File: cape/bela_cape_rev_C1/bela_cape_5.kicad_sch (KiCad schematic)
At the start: 26 parts, among them IC1 TLV320AIC3104, IC2 MIC5317

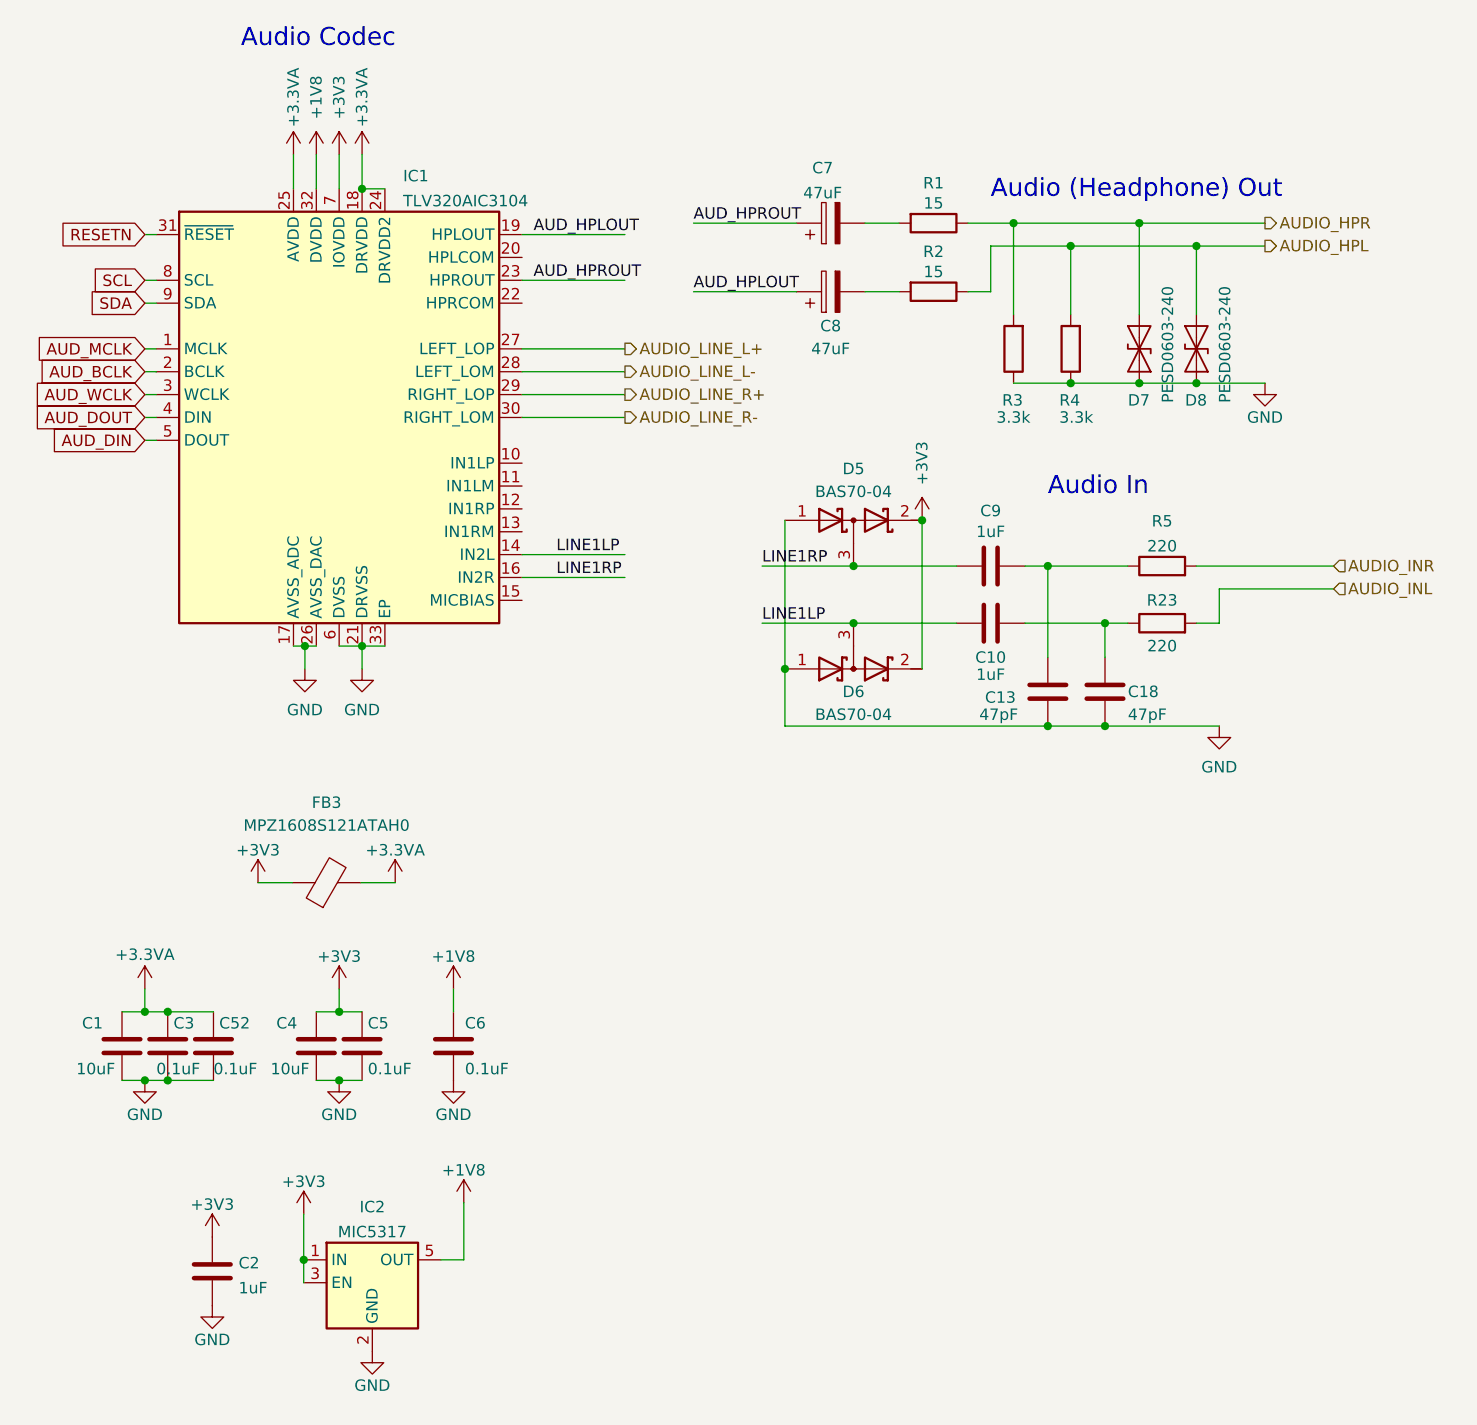
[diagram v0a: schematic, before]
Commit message: More C1 cape routing
(cherry picked from commit db7d999e21b46c22925661ce0002776775f31ffd)
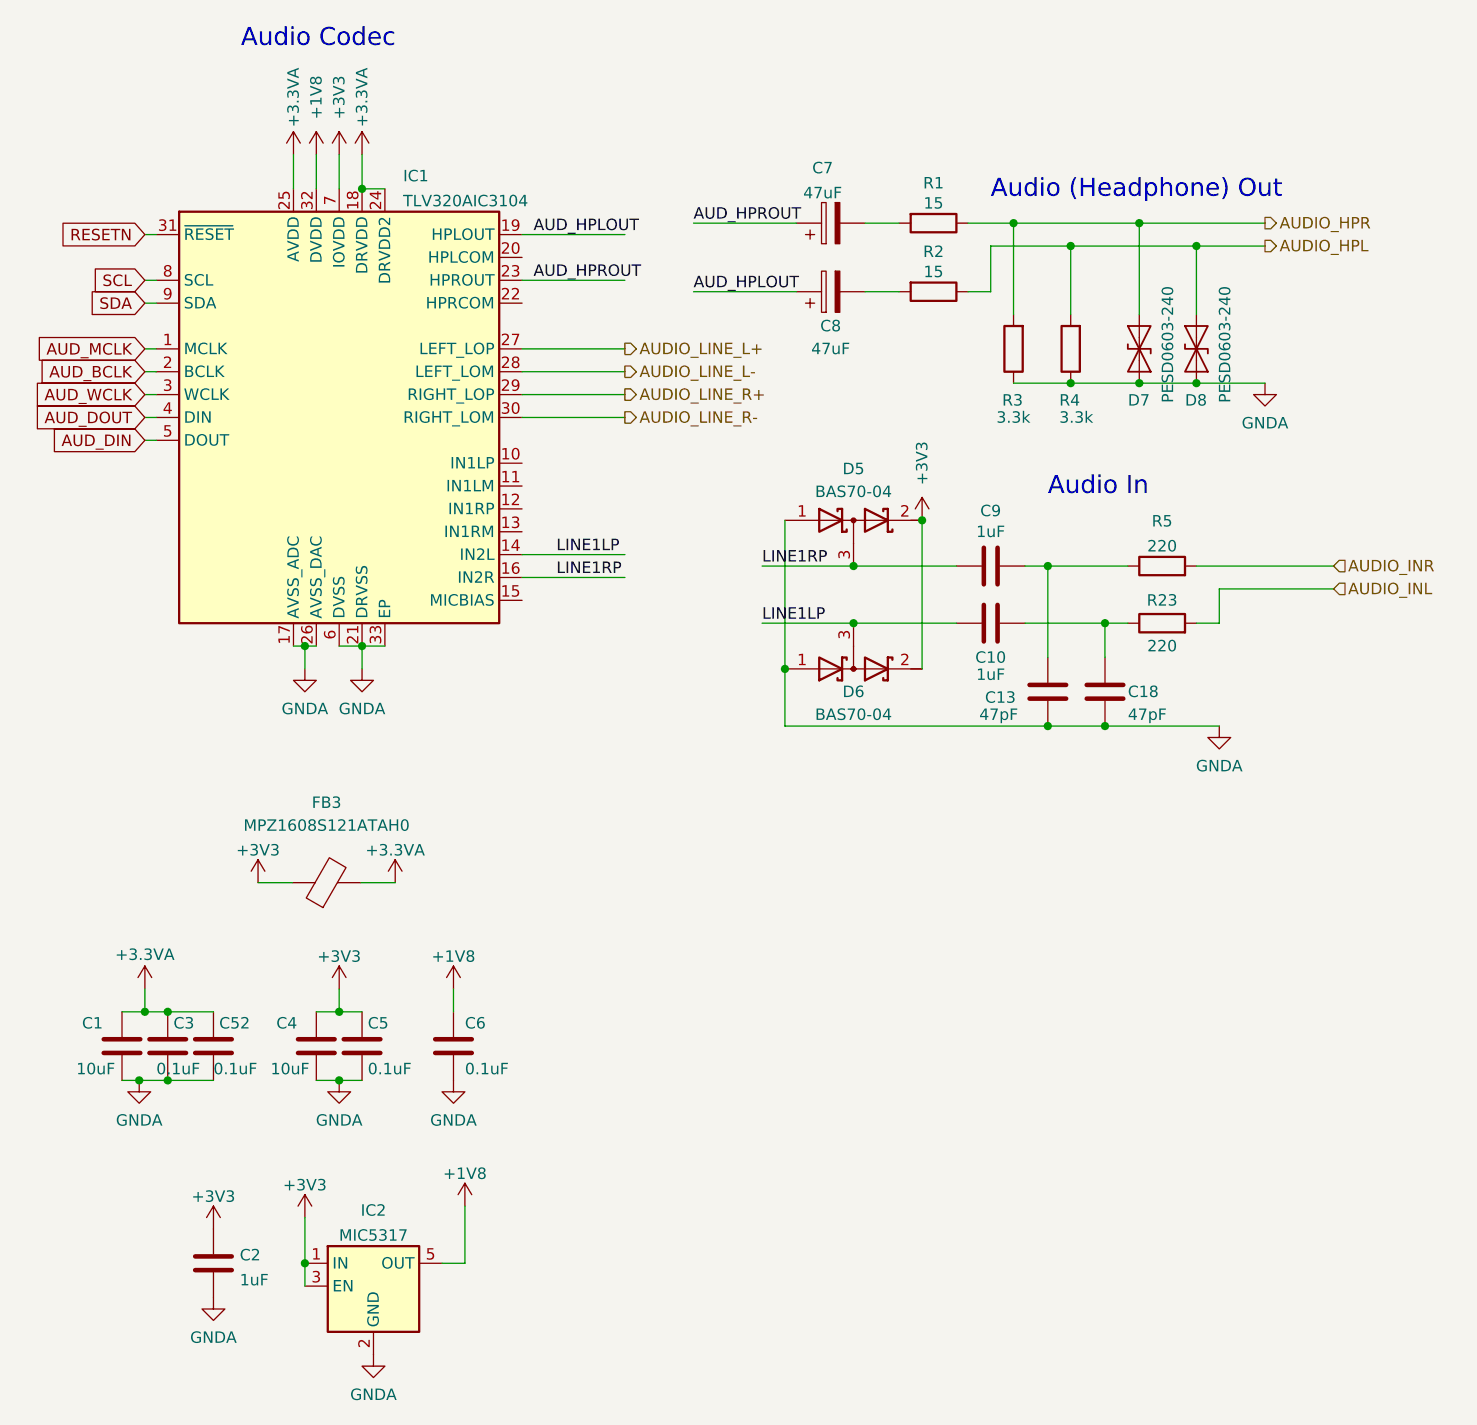
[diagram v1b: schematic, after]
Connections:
- net GND renamed GNDA
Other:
- moved on the sheet: C2

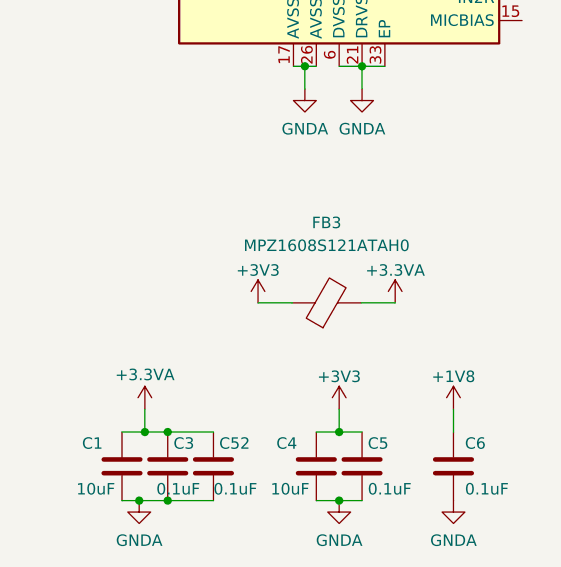
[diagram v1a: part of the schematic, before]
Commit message: Further routing on C1 cape
(cherry picked from commit 232a25b01e013bf194cdc3a343766aa7b43870aa)
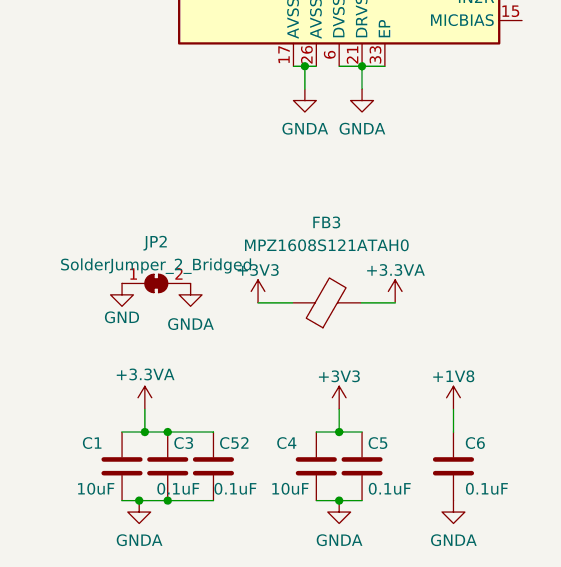
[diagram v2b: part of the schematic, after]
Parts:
- added JP2: SolderJumper_2_Bridged, Jumper:SolderJumper-2_P1.3mm_Bridged_Pad1.0x1.5mm, symbol Jumper:SolderJumper_2_Bridged
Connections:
- net GNDA: now also JP2.2 (B)
- new net GND: JP2.1 (A)
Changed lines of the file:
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@@
+    (pin "2")
+  )
+  (symbol (lib_id "Jumper:SolderJumper_2_Bridged") (at 31.75 111.76 0) (unit 1)
+    (in_bom yes) (on_board yes) (fields_autoplaced)
+    (property "Reference" "JP2" (id 0) (at 31.75 107.1712 0))
+    (property "Value" "SolderJumper_2_Bridged" (id 1) (at 31.75 109.7081 0))
+    (property "Footprint" "Jumper:SolderJumper-2_P1.3mm_Bridged_Pad1.0x1.5mm" (id 2) (at 31.75 111.76 0)
+      (effects (font (size 1.27 1.27)) hide)
+    )
+    (property "Datasheet" "~" (id 3) (at 31.75 111.76 0)
+      (effects (font (size 1.27 1.27)) hide)
+    )
+    (pin "1")
     (pin "2")
   )
@@
     (pin "1")
   )
+  (symbol (lib_id "power:GNDA") (at 35.56 111.76 0) (unit 1)
+    (in_bom yes) (on_board yes)
+    (property "Reference" "#PWR0163" (id 0) (at 35.56 118.11 0)
+      (effects (font (size 1.27 1.27)) hide)
+    )
+    (property "Value" "GNDA" (id 1) (at 35.56 116.3225 0))
+    (property "Footprint" "" (id 2) (at 35.56 111.76 0)
+      (effects (font (size 1.27 1.27)) hide)
+    )
+    (property "Datasheet" "" (id 3) (at 35.56 111.76 0)
+      (effects (font (size 1.27 1.27)) hide)
+    )
+    (pin "1")
+  )
   (symbol (lib_id "Device:R") (at 127 54.61 180) (unit 1)
     (in_bom yes) (on_board yes)
@@
     (pin "2")
   )
+  (symbol (lib_id "power:GND") (at 27.94 111.76 0) (mirror y) (unit 1)
+    (in_bom yes) (on_board yes)
+    (property "Reference" "#PWR0164" (id 0) (at 27.94 118.11 0)
+      (effects (font (size 1.27 1.27)) hide)
+    )
+    (property "Value" "GND" (id 1) (at 27.94 115.57 0))
+    (property "Footprint" "" (id 2) (at 27.94 111.76 0)
+      (effects (font (size 1.27 1.27)) hide)
+    )
+    (property "Datasheet" "" (id 3) (at 27.94 111.76 0)
+      (effects (font (size 1.27 1.27)) hide)
+    )
+    (pin "1")
+  )
   (symbol (lib_id "power:+3.3VA") (at 30.48 125.73 0) (unit 1)

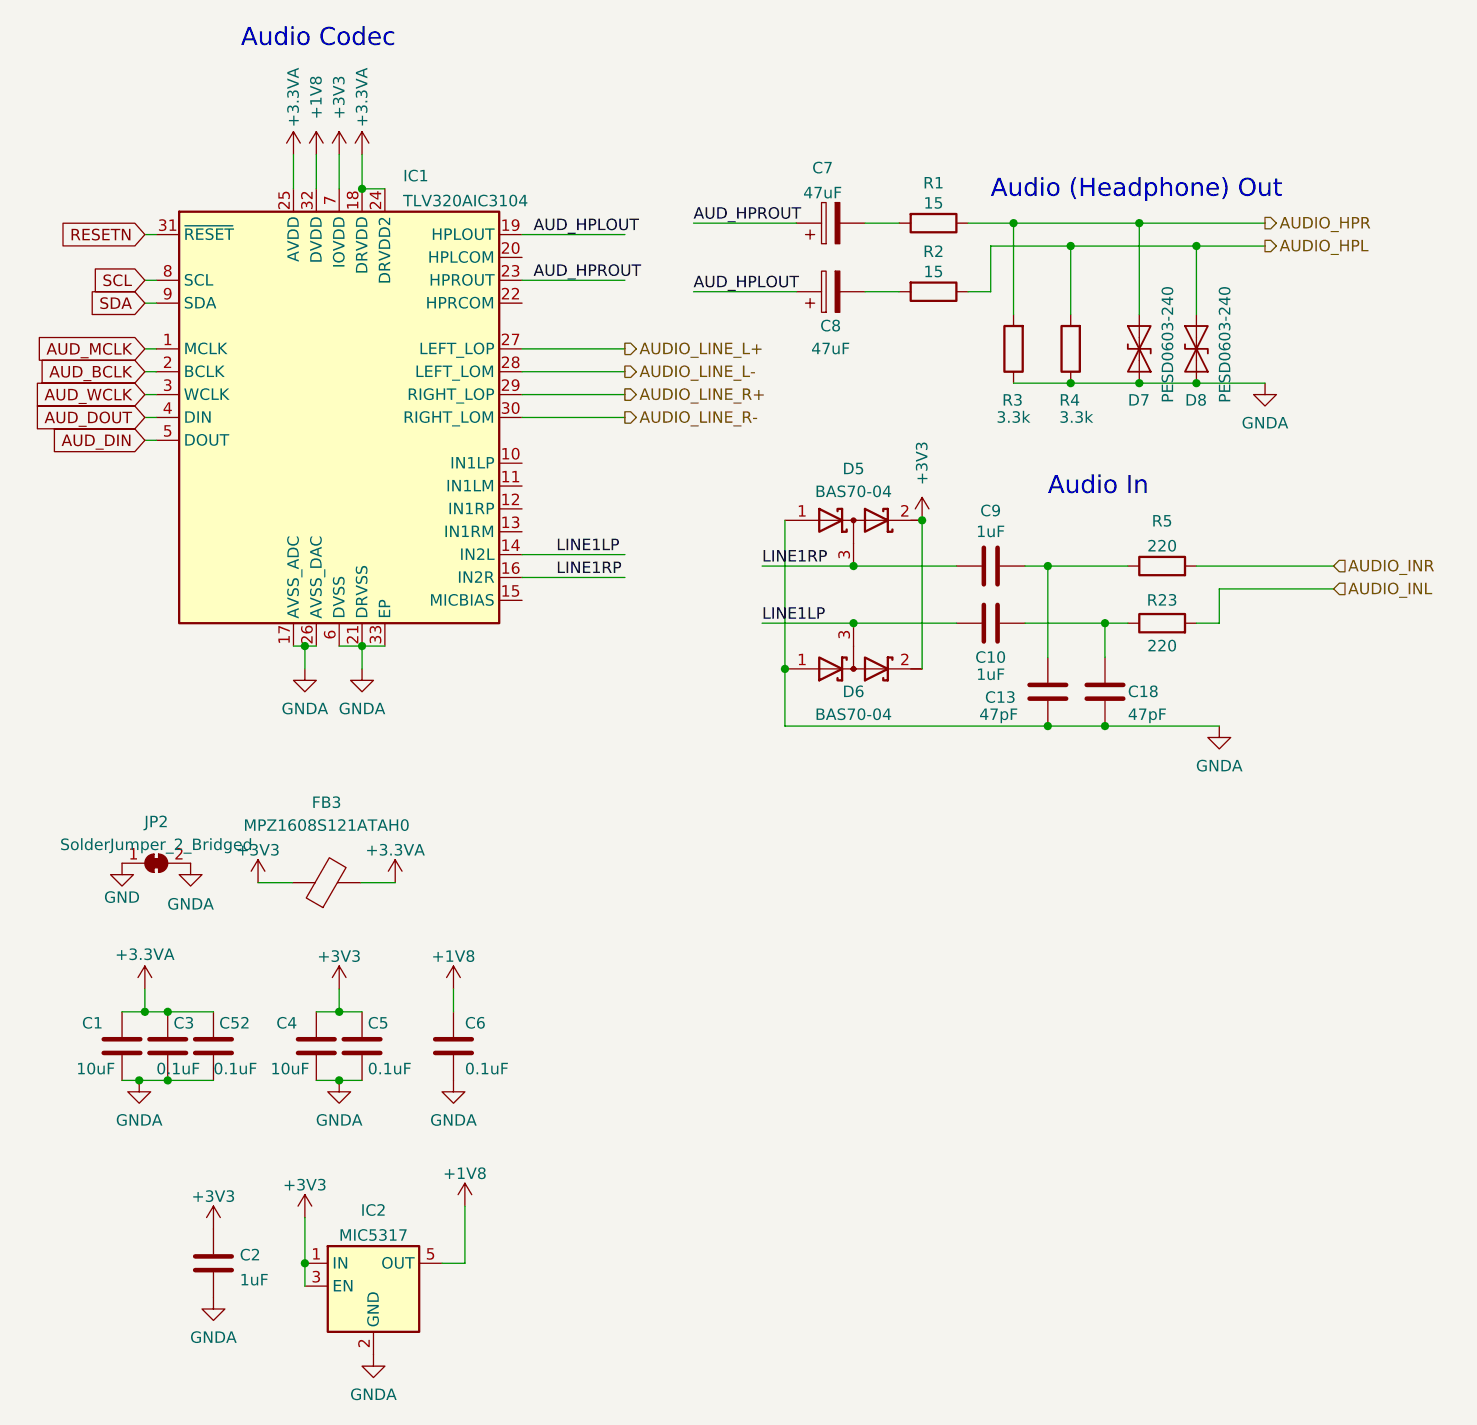
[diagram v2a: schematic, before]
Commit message: Bela cape C1: renumber components
(cherry picked from commit 6ebfe9c44bb7559ffb4c9dbd092e49803523e6a1)
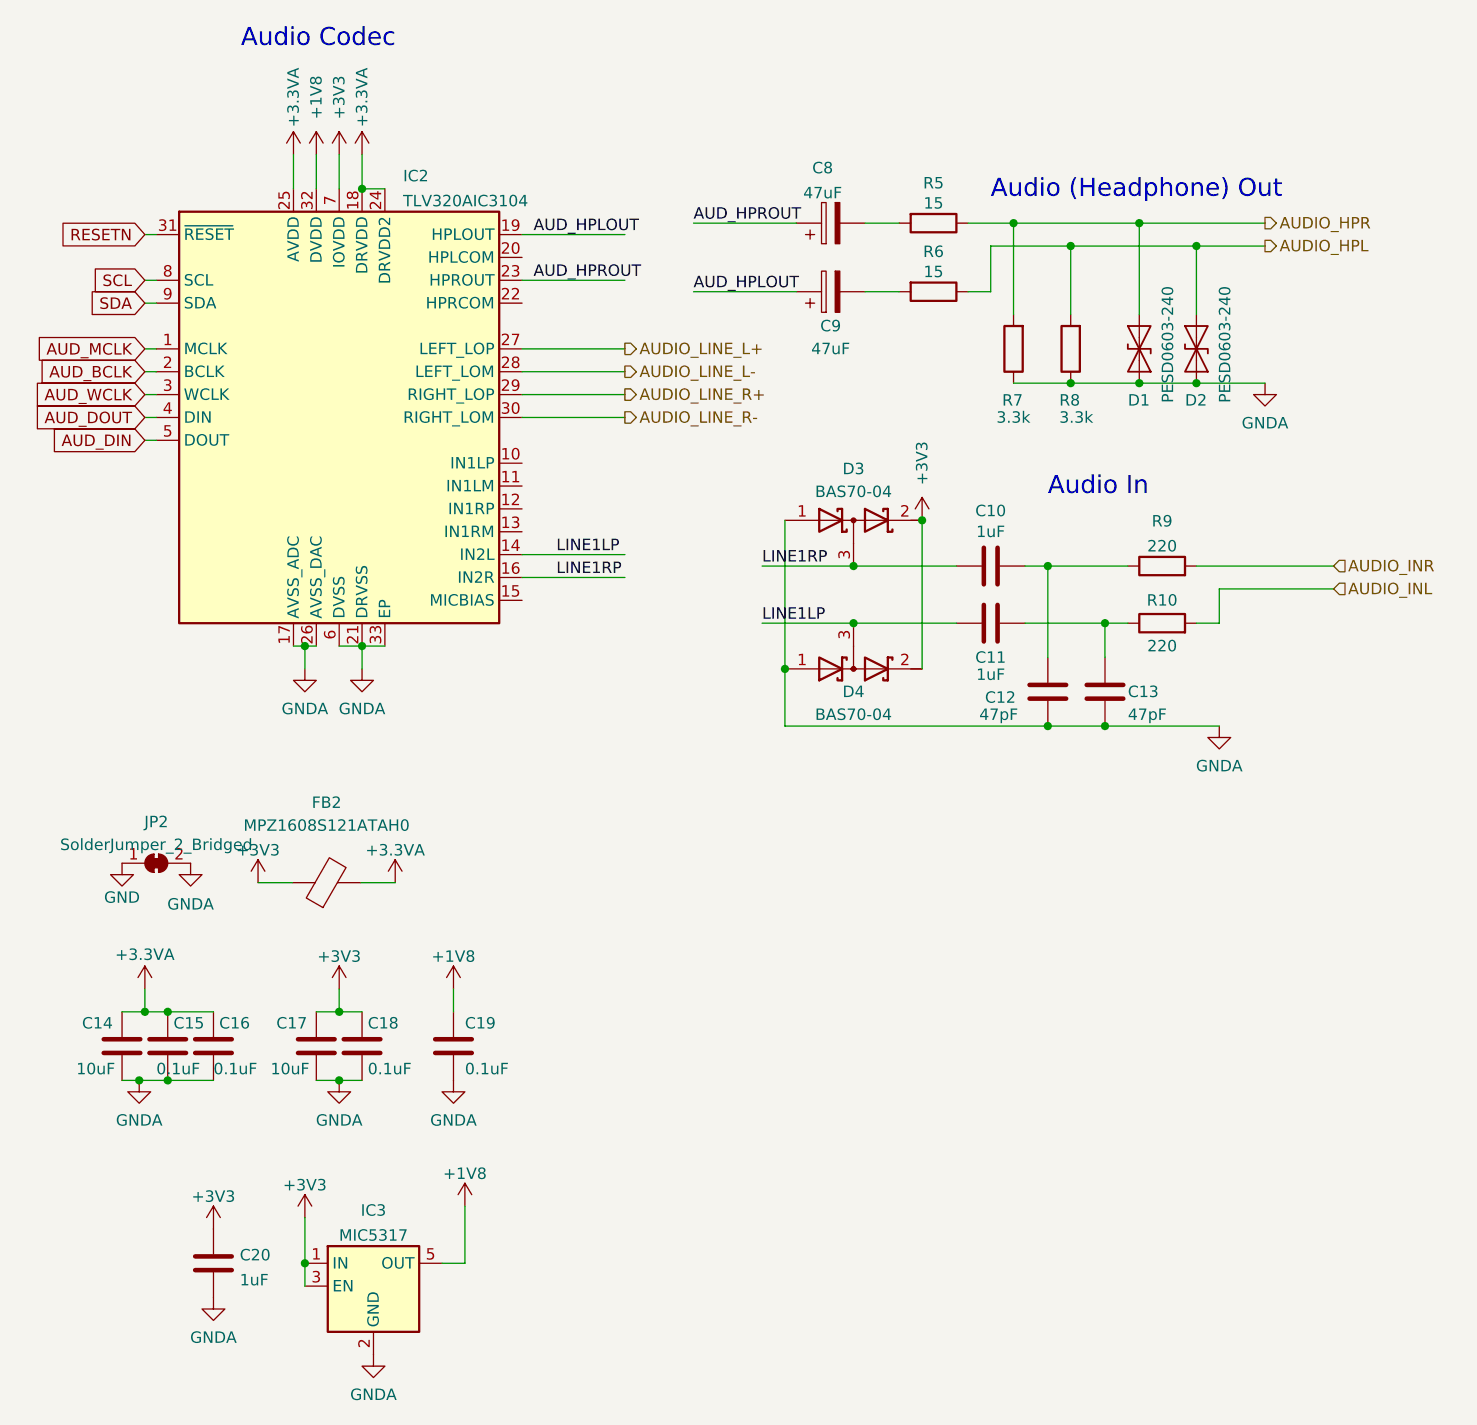
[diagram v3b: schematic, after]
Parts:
- renumbered C9 to C10, C10 to C11, C13 to C12, C18 to C13, C1 to C14, C3 to C15, C52 to C16, C4 to C17, C5 to C18, C6 to C19, C2 to C20, C7 to C8, C8 to C9, D7 to D1, D8 to D2, D5 to D3, D6 to D4, FB3 to FB2, IC1 to IC2, IC2 to IC3, R23 to R10, R1 to R5, R2 to R6, R3 to R7, R4 to R8, R5 to R9
